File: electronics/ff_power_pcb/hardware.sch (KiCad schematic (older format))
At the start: 70 parts, among them J1 Conn_01x01_Female, J2 Conn_01x01_Female, U3 TPS62095RGTR, U4 TPS62095RGTR, U5 TPS62095RGTR, U6 TPS62095RGTR, U7 AP131-25

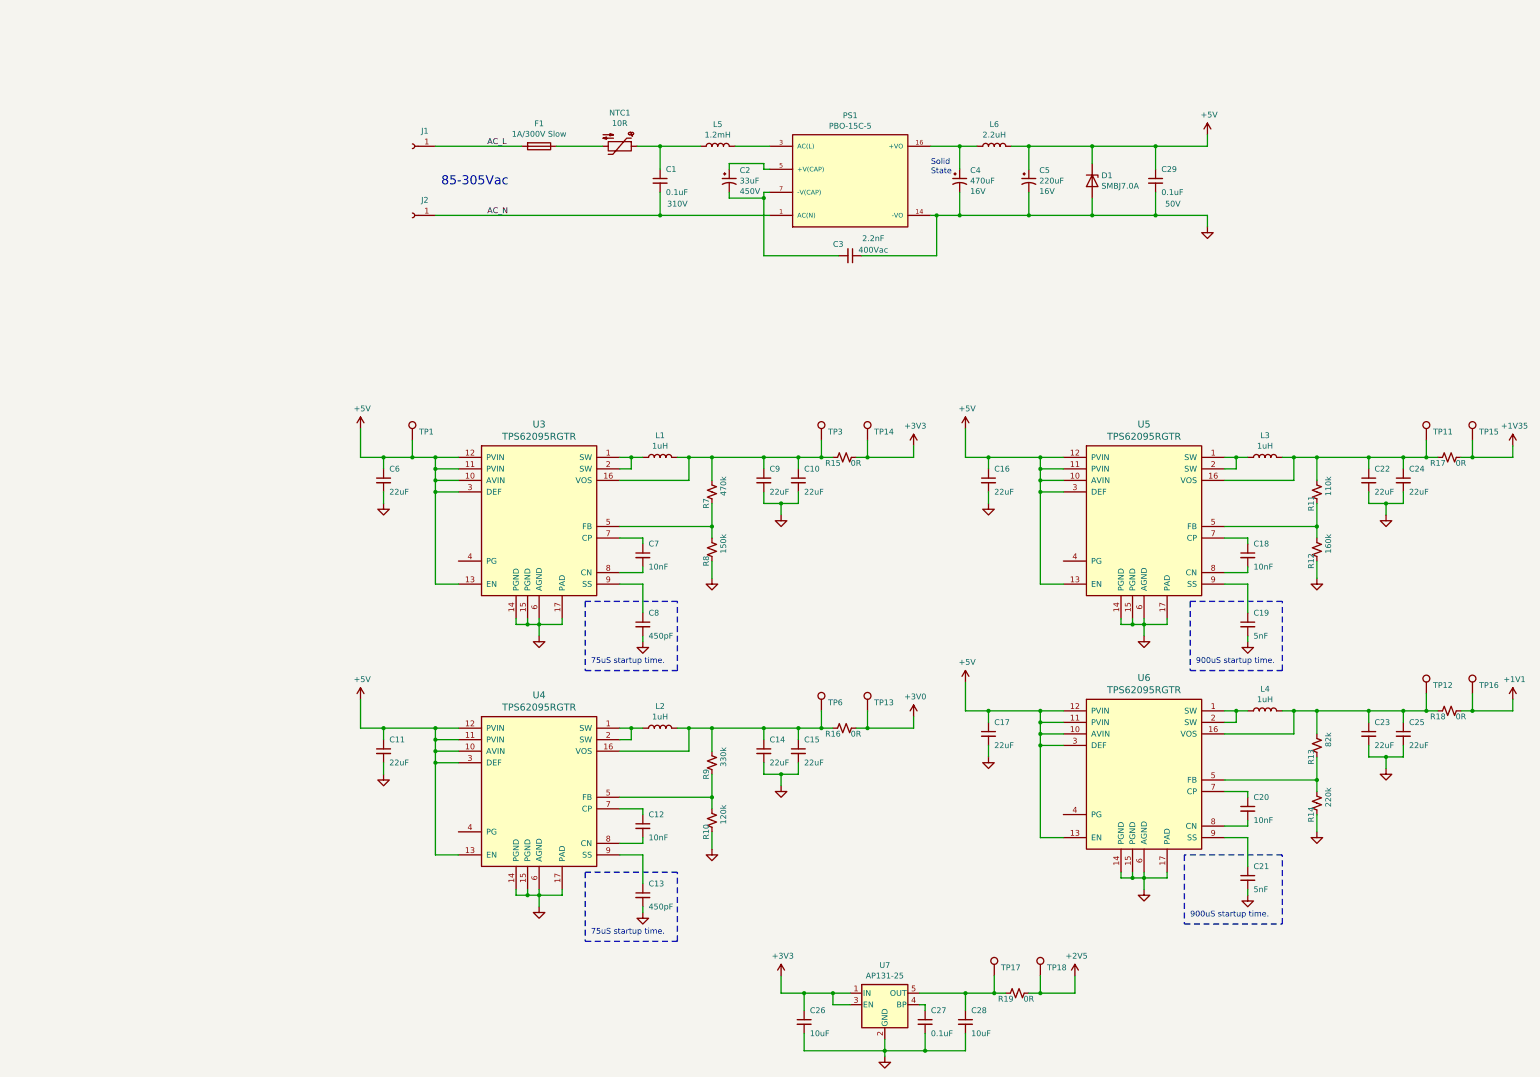
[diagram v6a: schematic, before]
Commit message: Dropped in the power board with all the new components.
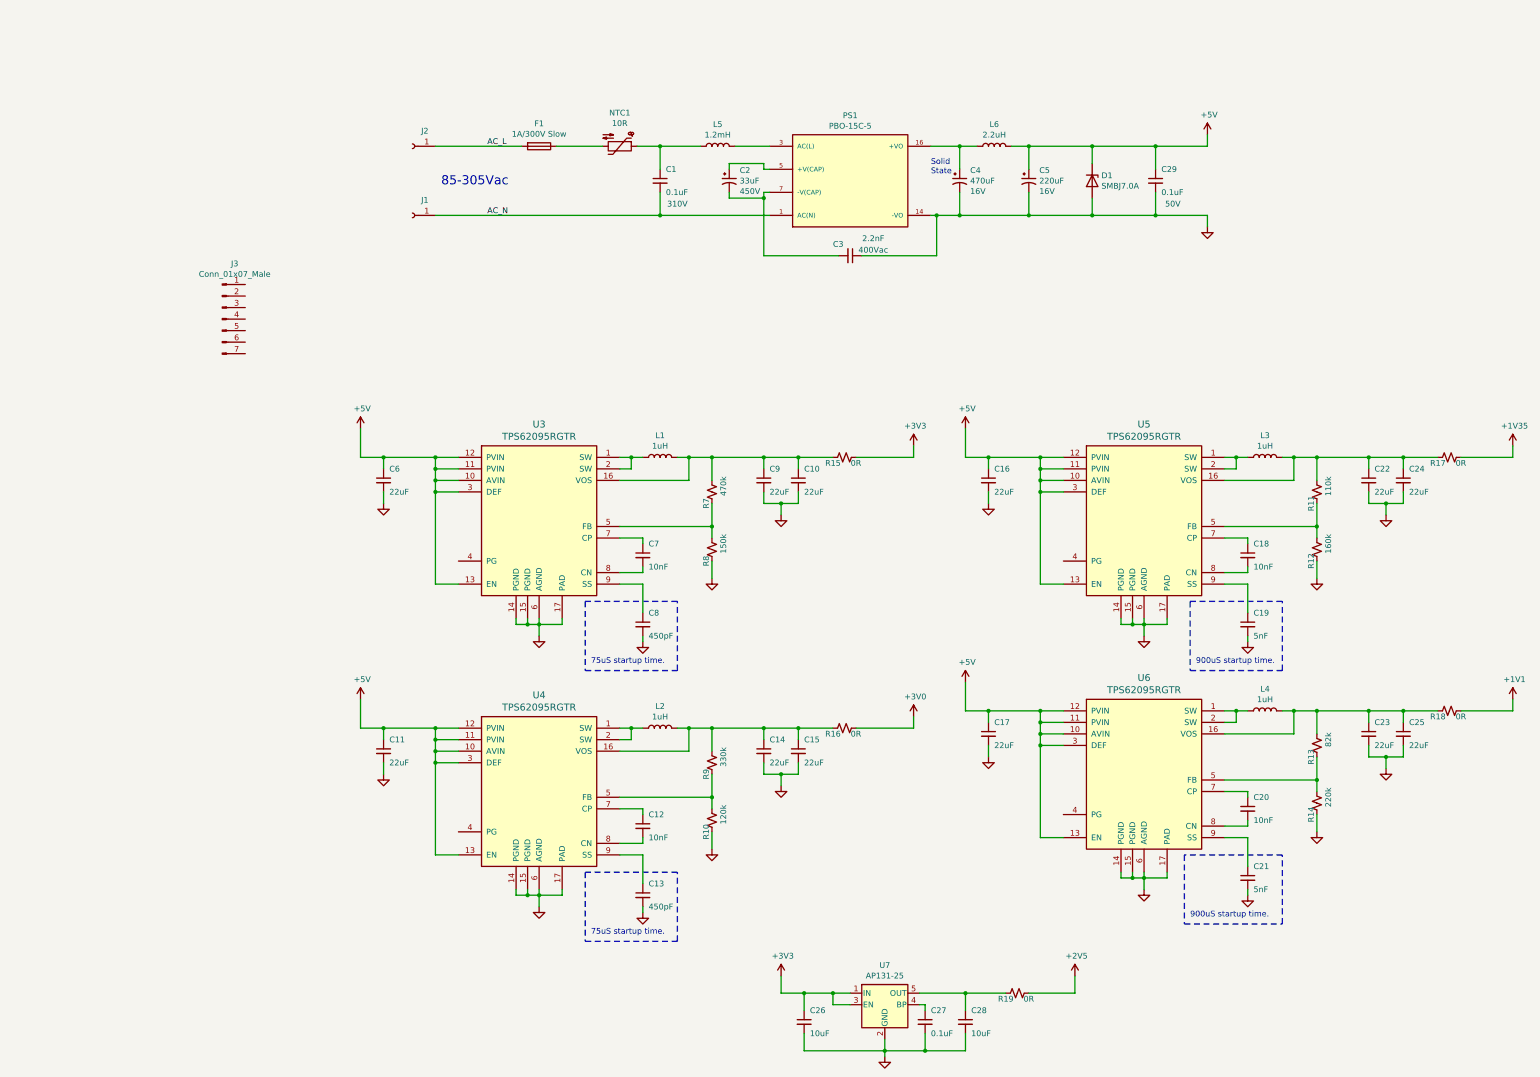
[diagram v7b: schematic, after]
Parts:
- removed TP1, TP11, TP12, TP13, TP14, TP15, TP16, TP17, TP18, TP3, TP6: TestPoint, TestPoint:TestPoint_Pad_1.0x1.0mm, symbol Connector:TestPoint
- added J3: Conn_01x07_Male, Connector_PinSocket_2.54mm:PinSocket_1x07_P2.54mm_Vertical, symbol Connector:Conn_01x07_Male
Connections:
- net AC_L: now also J2.1 (Pin_1); no longer J1.1 (Pin_1)
- net AC_N: now also J1.1 (Pin_1); no longer J2.1 (Pin_1)
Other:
- moved on the sheet: J1, J2
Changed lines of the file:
@@
-$EndComp
-$Comp
-L Connector:TestPoint TP3
-U 1 1 60A0B93D
-P 7800 4450
-F 0 "TP3" H 7858 4522 50  0000 L CNN
-F 1 "TestPoint" H 7858 4477 50  0001 L CNN
-F 2 "TestPoint:TestPoint_Pad_1.0x1.0mm" H 8000 4450 50  0001 C CNN
-F 3 "~" H 8000 4450 50  0001 C CNN
-F 4 "~" H 7858 4622 50  0001 C CNN "MPN"
-F 5 "~" H 7858 4622 50  0001 C CNN "Tolerance"
-	1    7800 4450
-	1    0    0    -1
-$EndComp
-$Comp
-L Connector:TestPoint TP1
-U 1 1 60A1B174
-P 4250 4450
-F 0 "TP1" H 4308 4522 50  0000 L CNN
-F 1 "TestPoint" H 4308 4477 50  0001 L CNN
-F 2 "TestPoint:TestPoint_Pad_1.0x1.0mm" H 4450 4450 50  0001 C CNN
-F 3 "~" H 4450 4450 50  0001 C CNN
-F 4 "~" H 4308 4622 50  0001 C CNN "MPN"
-F 5 "~" H 4308 4622 50  0001 C CNN "Tolerance"
-	1    4250 4450
-	1    0    0    -1
 $EndComp
 $Comp
@@
 $EndComp
 $Comp
-L Connector:TestPoint TP6
-U 1 1 60A665A3
-P 7800 6800
-F 0 "TP6" H 7858 6872 50  0000 L CNN
-F 1 "TestPoint" H 7858 6827 50  0001 L CNN
-F 2 "TestPoint:TestPoint_Pad_1.0x1.0mm" H 8000 6800 50  0001 C CNN
-F 3 "~" H 8000 6800 50  0001 C CNN
-F 4 "~" H 7858 6972 50  0001 C CNN "MPN"
-F 5 "~" H 7858 6972 50  0001 C CNN "Tolerance"
-	1    7800 6800
-	1    0    0    -1
-$EndComp
-$Comp
 L power:+5V #PWR029
 U 1 1 60A8945F
@@
 $EndComp
 $Comp
-L Connector:TestPoint TP11
-U 1 1 60A8950F
-P 13050 4450
-F 0 "TP11" H 13108 4522 50  0000 L CNN
-F 1 "TestPoint" H 13108 4477 50  0001 L CNN
-F 2 "TestPoint:TestPoint_Pad_1.0x1.0mm" H 13250 4450 50  0001 C CNN
-F 3 "~" H 13250 4450 50  0001 C CNN
-F 4 "~" H 13108 4622 50  0001 C CNN "MPN"
-F 5 "~" H 13108 4622 50  0001 C CNN "Tolerance"
-	1    13050 4450
-	1    0    0    -1
-$EndComp
-$Comp
 L power:+5V #PWR030
 U 1 1 60C53071
@@
 F 3 "" H 11500 8400 50  0001 C CNN
 	1    11500 8400
-	1    0    0    -1
-$EndComp
-$Comp
-L Connector:TestPoint TP12
-U 1 1 60C53121
-P 13050 6650
-F 0 "TP12" H 13108 6722 50  0000 L CNN
-F 1 "TestPoint" H 13108 6677 50  0001 L CNN
-F 2 "TestPoint:TestPoint_Pad_1.0x1.0mm" H 13250 6650 50  0001 C CNN
-F 3 "~" H 13250 6650 50  0001 C CNN
-F 4 "~" H 13108 6822 50  0001 C CNN "MPN"
-F 5 "~" H 13108 6822 50  0001 C CNN "Tolerance"
-	1    13050 6650
 	1    0    0    -1
 $EndComp
@@
 $EndComp
 $Comp
-L Connector:TestPoint TP15
-U 1 1 606511D4
-P 13450 4450
-F 0 "TP15" H 13508 4522 50  0000 L CNN
-F 1 "TestPoint" H 13508 4477 50  0001 L CNN
-F 2 "TestPoint:TestPoint_Pad_1.0x1.0mm" H 13650 4450 50  0001 C CNN
-F 3 "~" H 13650 4450 50  0001 C CNN
-F 4 "~" H 13508 4622 50  0001 C CNN "MPN"
-F 5 "~" H 13508 4622 50  0001 C CNN "Tolerance"
-	1    13450 4450
-	1    0    0    -1
-$EndComp
-$Comp
-L Connector:TestPoint TP16
-U 1 1 606AB258
-P 13450 6650
-F 0 "TP16" H 13508 6722 50  0000 L CNN
-F 1 "TestPoint" H 13508 6677 50  0001 L CNN
-F 2 "TestPoint:TestPoint_Pad_1.0x1.0mm" H 13650 6650 50  0001 C CNN
-F 3 "~" H 13650 6650 50  0001 C CNN
-F 4 "~" H 13508 6822 50  0001 C CNN "MPN"
-F 5 "~" H 13508 6822 50  0001 C CNN "Tolerance"
-	1    13450 6650
-	1    0    0    -1
-$EndComp
-$Comp
-L Connector:TestPoint TP13
-U 1 1 606C8854
-P 8200 6800
-F 0 "TP13" H 8258 6872 50  0000 L CNN
-F 1 "TestPoint" H 8258 6827 50  0001 L CNN
-F 2 "TestPoint:TestPoint_Pad_1.0x1.0mm" H 8400 6800 50  0001 C CNN
-F 3 "~" H 8400 6800 50  0001 C CNN
-F 4 "~" H 8258 6972 50  0001 C CNN "MPN"
-F 5 "~" H 8258 6972 50  0001 C CNN "Tolerance"
-	1    8200 6800
-	1    0    0    -1
-$EndComp
-$Comp
-L Connector:TestPoint TP14
-U 1 1 60704DE7
-P 8200 4450
-F 0 "TP14" H 8258 4522 50  0000 L CNN
-F 1 "TestPoint" H 8258 4477 50  0001 L CNN
-F 2 "TestPoint:TestPoint_Pad_1.0x1.0mm" H 8400 4450 50  0001 C CNN
-F 3 "~" H 8400 4450 50  0001 C CNN
-F 4 "~" H 8258 4622 50  0001 C CNN "MPN"
-F 5 "~" H 8258 4622 50  0001 C CNN "Tolerance"
-	1    8200 4450
-	1    0    0    -1
-$EndComp
-$Comp
 L Regulator_Linear:AP131-25 U7
 U 1 1 60A041CF
@@
 $EndComp
 $Comp
-L Connector:TestPoint TP17
-U 1 1 60B002CC
-P 9300 9100
-F 0 "TP17" H 9358 9172 50  0000 L CNN
-F 1 "TestPoint" H 9358 9127 50  0001 L CNN
-F 2 "TestPoint:TestPoint_Pad_1.0x1.0mm" H 9500 9100 50  0001 C CNN
-F 3 "~" H 9500 9100 50  0001 C CNN
-F 4 "~" H 9358 9272 50  0001 C CNN "MPN"
-F 5 "~" H 9358 9272 50  0001 C CNN "Tolerance"
-	1    9300 9100
-	1    0    0    -1
-$EndComp
-$Comp
-L Connector:TestPoint TP18
-U 1 1 60B002D3
-P 9700 9100
-F 0 "TP18" H 9758 9172 50  0000 L CNN
-F 1 "TestPoint" H 9758 9127 50  0001 L CNN
-F 2 "TestPoint:TestPoint_Pad_1.0x1.0mm" H 9900 9100 50  0001 C CNN
-F 3 "~" H 9900 9100 50  0001 C CNN
-F 4 "~" H 9758 9272 50  0001 C CNN "MPN"
-F 5 "~" H 9758 9272 50  0001 C CNN "Tolerance"
-	1    9700 9100
-	1    0    0    -1
-$EndComp
-$Comp
 L TI:TPS62095 U5
 U 1 1 60A894ED
@@
 	4000 4700 4000 4600
 Wire Wire Line
-	4000 4600 4250 4600
-Wire Wire Line
 	4000 4900 4000 5000
 Wire Wire Line
 	6250 6200 6250 6150
 Wire Wire Line
-	7800 4600 7800 4450
-Wire Wire Line
-	4250 4600 4250 4450
-Wire Wire Line
-	4250 4600 4450 4600
-Wire Wire Line
 	3800 6700 3800 6950
 Wire Wire Line
@@
 Wire Wire Line
 	7300 6950 7600 6950
-Wire Wire Line
-	7600 6950 7800 6950
 Wire Wire Line
 	8600 6950 8600 6850
@@
 	6250 8550 6250 8500
 Wire Wire Line
-	7800 6950 7800 6800
-Wire Wire Line
 	9050 4350 9050 4600
 Wire Wire Line
@@
 	11500 6200 11500 6150
 Wire Wire Line
-	13050 4600 13050 4450
-Wire Wire Line
 	9050 6550 9050 6800
 Wire Wire Line
@@
 Wire Wire Line
 	11500 8400 11500 8350
-Wire Wire Line
-	13050 6800 13050 6650
 Wire Notes Line
 	11800 8050 10950 8050
 Wire Wire Line
-	8100 4600 8200 4600
-Wire Wire Line
-	8100 6950 8200 6950
-Wire Wire Line
 	12100 4600 12550 4600
 Wire Wire Line
-	13450 4600 13450 4450
-Wire Wire Line
-	13350 4600 13450 4600
-Wire Wire Line
 	12100 6800 12550 6800
 Wire Wire Line
-	8200 6950 8200 6800
-Wire Wire Line
-	7800 6950 7900 6950
-Wire Wire Line
 	6850 6950 7300 6950
 Wire Wire Line
 	6850 4600 7300 4600
 Wire Wire Line
-	8200 4600 8200 4450
-Wire Wire Line
-	8200 6950 8600 6950
-Wire Wire Line
-	13450 6800 13450 6650
-Wire Wire Line
-	13350 6800 13450 6800
-Wire Wire Line
-	8200 4600 8600 4600
-Wire Wire Line
-	7800 4600 7900 4600
-Wire Wire Line
-	7600 4600 7800 4600
-Wire Wire Line
-	13050 4600 13150 4600
-Wire Wire Line
-	12850 4600 13050 4600
-Wire Wire Line
-	13450 4600 13800 4600
-Wire Wire Line
-	13050 6800 13150 6800
-Wire Wire Line
-	12850 6800 13050 6800
-Wire Wire Line
-	13450 6800 13800 6800
-Wire Wire Line
 	8050 9250 7900 9250
 Wire Wire Line
@@
 	8700 9750 8350 9750
 Wire Wire Line
-	9050 9250 9300 9250
-Wire Wire Line
 	10000 9250 10000 9100
-Wire Wire Line
-	9600 9250 9700 9250
-Wire Wire Line
-	9300 9250 9300 9100
-Wire Wire Line
-	9700 9250 9700 9100
-Wire Wire Line
-	9700 9250 10000 9250
-Wire Wire Line
-	9300 9250 9400 9250
 Wire Wire Line
 	8050 9350 7900 9350
@@
 Connection ~ 7600 4600
 Connection ~ 4000 4600
-Connection ~ 4250 4600
 Connection ~ 4450 7050
 Connection ~ 4450 7150
@@
 Connection ~ 12850 6800
 Connection ~ 9250 6800
-Connection ~ 7800 6950
-Connection ~ 8200 6950
-Connection ~ 8200 4600
-Connection ~ 7800 4600
-Connection ~ 13050 4600
-Connection ~ 13450 4600
-Connection ~ 13050 6800
-Connection ~ 13450 6800
 Connection ~ 7650 9250
 Connection ~ 8350 9750
 Connection ~ 8700 9750
 Connection ~ 9050 9250
-Connection ~ 9700 9250
-Connection ~ 9300 9250
 Connection ~ 7900 9250
 $Comp
@@
 L Connector:Conn_01x01_Female J1
 U 1 1 60CFC609
+P 4250 2500
+F 0 "J1" H 4142 2367 50  0000 C CNN
+F 1 "Conn_01x01_Female" H 4142 2366 50  0001 C CNN
+F 2 "Connector_PinHeader_2.54mm:PinHeader_1x01_P2.54mm_Vertical" H 4250 2500 50  0001 C CNN
+F 3 "~" H 4250 2500 50  0001 C CNN
+	1    4250 2500
+	-1   0    0    1
+$EndComp
+$Comp
+L Connector:Conn_01x01_Female J2
+U 1 1 60CFCE80
 P 4250 1900
-F 0 "J1" H 4142 1767 50  0000 C CNN
+F 0 "J2" H 4142 1767 50  0000 C CNN
 F 1 "Conn_01x01_Female" H 4142 1766 50  0001 C CNN
 F 2 "Connector_PinHeader_2.54mm:PinHeader_1x01_P2.54mm_Vertical" H 4250 1900 50  0001 C CNN
@@
 	-1   0    0    1
 $EndComp
-$Comp
-L Connector:Conn_01x01_Female J2
-U 1 1 60CFCE80
-P 4250 2500
-F 0 "J2" H 4142 2367 50  0000 C CNN
-F 1 "Conn_01x01_Female" H 4142 2366 50  0001 C CNN
-F 2 "Connector_PinHeader_2.54mm:PinHeader_1x01_P2.54mm_Vertical" H 4250 2500 50  0001 C CNN
-F 3 "~" H 4250 2500 50  0001 C CNN
-	1    4250 2500
-	-1   0    0    1
+Wire Wire Line
+	4000 4600 4450 4600
+Wire Wire Line
+	7600 4600 7900 4600
+Wire Wire Line
+	8100 4600 8600 4600
+Wire Wire Line
+	12850 4600 13150 4600
+Wire Wire Line
+	13350 4600 13800 4600
+Wire Wire Line
+	7600 6950 7900 6950
+Wire Wire Line
+	8100 6950 8600 6950
+Wire Wire Line
+	12850 6800 13150 6800
+Wire Wire Line
+	13350 6800 13800 6800
+Wire Wire Line
+	9050 9250 9400 9250
+Wire Wire Line
+	9600 9250 10000 9250
+$Comp
+L Connector:Conn_01x07_Male J3
+U 1 1 60CBBBFE
+P 2600 3400
+F 0 "J3" H 2708 3881 50  0000 C CNN
+F 1 "Conn_01x07_Male" H 2708 3790 50  0000 C CNN
+F 2 "Connector_PinSocket_2.54mm:PinSocket_1x07_P2.54mm_Vertical" H 2600 3400 50  0001 C CNN
+F 3 "~" H 2600 3400 50  0001 C CNN
+	1    2600 3400
+	1    0    0    -1
 $EndComp
 $EndSCHEMATC

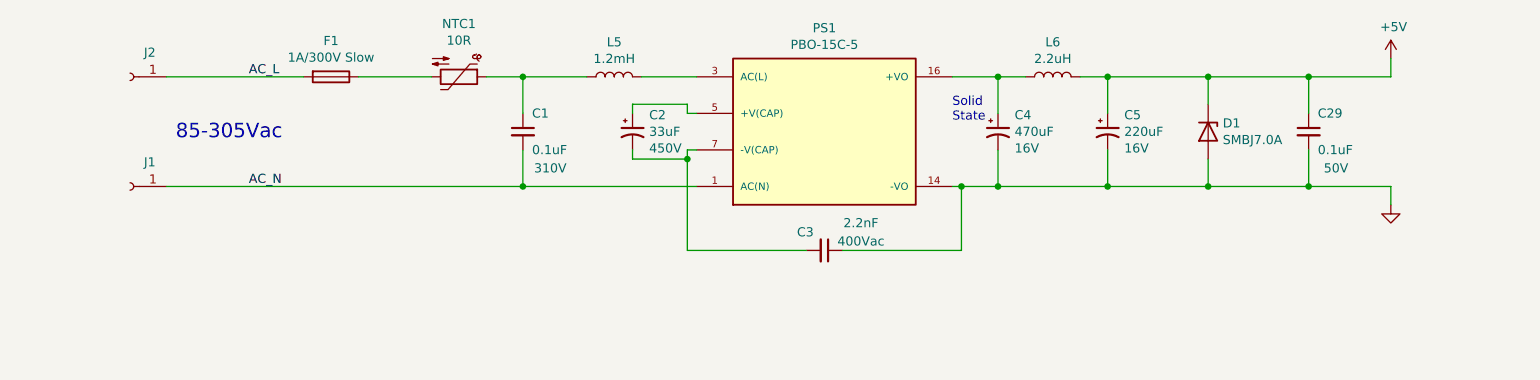
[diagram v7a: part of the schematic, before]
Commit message: Changed out the 15W supply for a 5W.
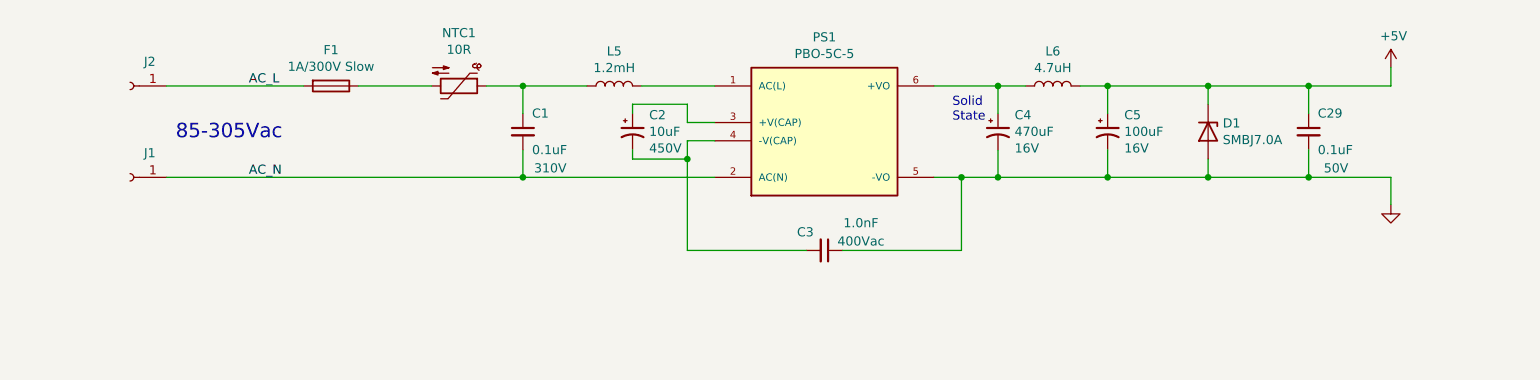
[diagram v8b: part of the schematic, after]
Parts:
- removed PS1: PBO-15C-5, CUI:CONV_PBO-15C-5, symbol CUI:PBO-15C-5
- added PS1: PBO-5C-5, CUI:CONV_PBO-5C-12, symbol CUI:PBO-5C-12
- C2: value 33uF -> 10uF; footprint Capacitor_THT:C_Radial_D16.0mm_H25.0mm_P7.50mm -> Capacitor_THT:C_Radial_D12.5mm_H20.0mm_P5.00mm; MPN EEU-EE2W330S -> UVR2W100MHD
- C3: value 2.2nF -> 1.0nF; footprint Capacitor_SMD:C_1206_3216Metric -> (none); MPN 501R18W223KV4E -> (none)
- C5: value 220uF -> 100uF; footprint Capacitor_SMD:CP_Elec_8x10.5 -> Capacitor_SMD:CP_Elec_6.3x5.8; MPN EEE-HA1C221UP -> 16ML100MEFC6.3X7
- L6: value 2.2uH -> 4.7uH; footprint Inductor_SMD:L_Coilcraft_XxL4020 -> Inductor_SMD:L_Coilcraft_XxL4030; MPN XAL4020-222ME -> XAL4030-472ME
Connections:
- net AC_N: now also PS1.2 (AC(N))
- net GND: now also PS1.5 (-VO)
- net at C2.1: now also PS1.3 (+V(CAP))
- net at C2.2, C3.2: now also PS1.4 (-V(CAP))
- net at C4.1, L6.1: now also PS1.6 (+VO)
- net at L5.2: now also PS1.1 (AC(L))
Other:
- moved on the sheet: F1, J1, J2, L5, L6, NTC1
